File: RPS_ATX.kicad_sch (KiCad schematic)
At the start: 36 parts, among them J1 Fan_in, J13 Fan_out, J2 C1, J3 C2, J4 17.5V, J5 PS_OUT-, J6 PS_OUT+, J7 RPS_OUT+, J9 RPS_OUT-, Q1 AO3400A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

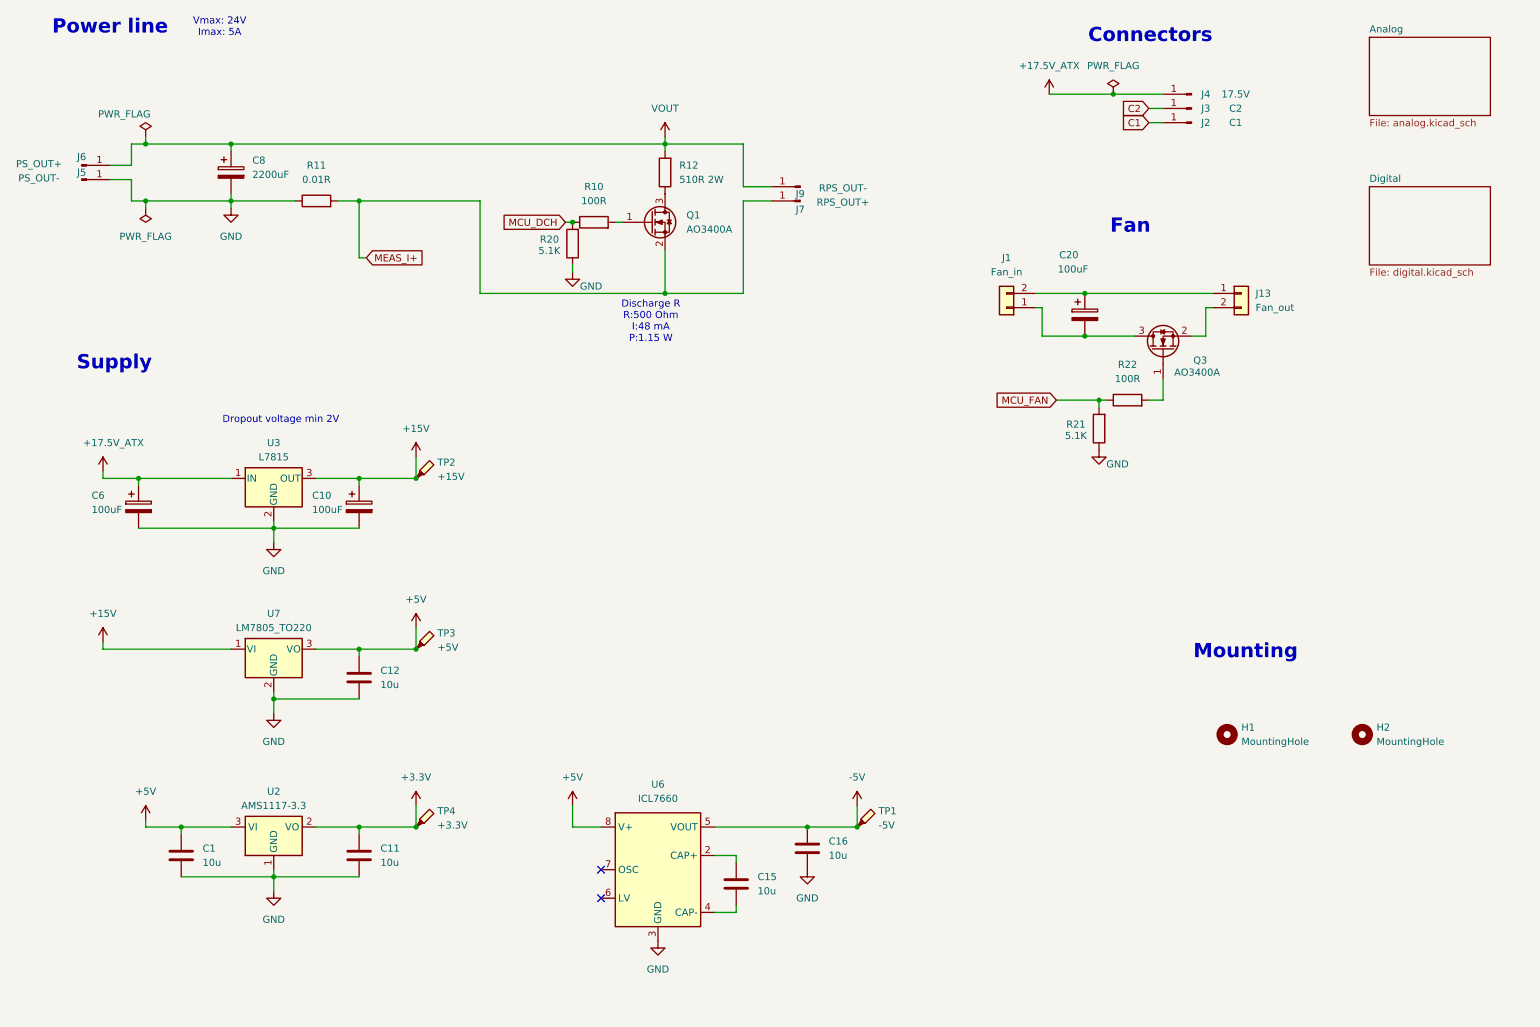
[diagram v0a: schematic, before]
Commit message: fan and temp sensor tracing
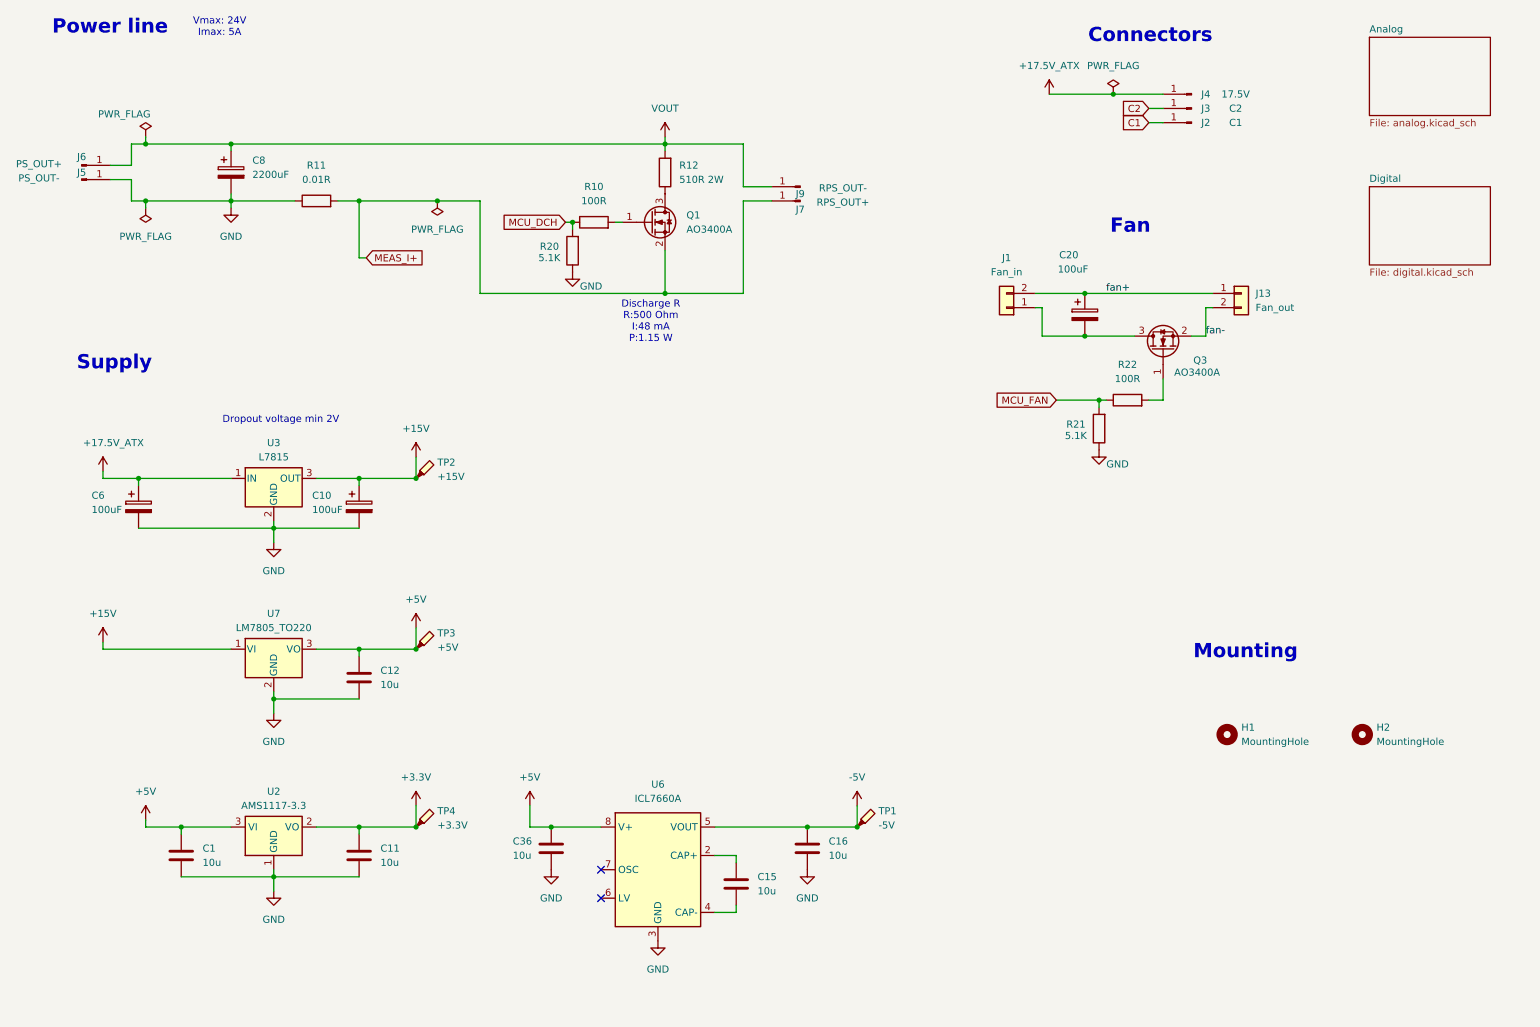
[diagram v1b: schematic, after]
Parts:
- added C36: 10u, Capacitor_SMD:C_1206_3216Metric_Pad1.33x1.80mm_HandSolder, symbol Device:C
- J1, J13: footprint Connector_PinHeader_2.54mm:PinHeader_1x02_P2.54mm_Vertical -> Connector_JST:JST_XH_B2B-XH-A_1x02_P2.50mm_Vertical
- U6: value ICL7660 -> ICL7660A
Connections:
- net +5V: now also C36.1
- net GND: now also C36.2
- net fan+: now reaches C20.1, J1.2 (Pin_2), J13.1 (Pin_1)
- net fan-: now reaches J13.2 (Pin_2), Q3.2 (S)
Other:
- moved on the sheet: R20

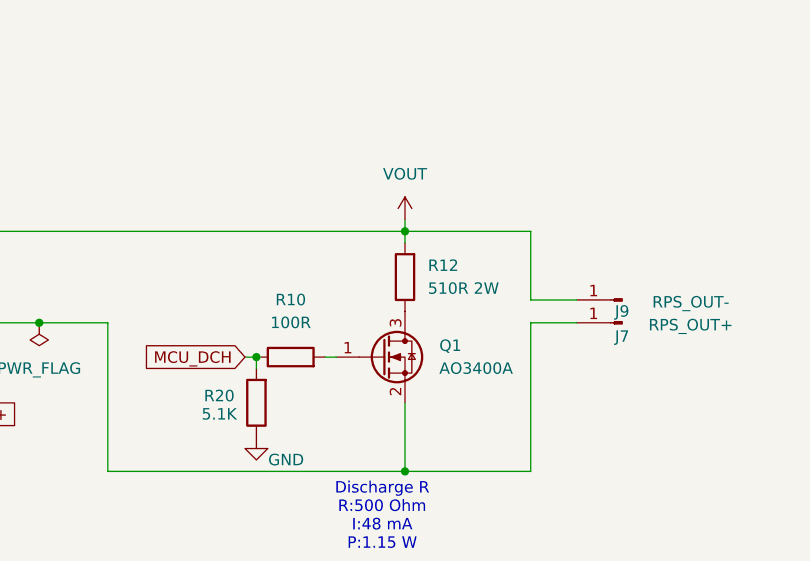
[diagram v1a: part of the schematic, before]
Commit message: minor changes (0805 for 0.1% R, new Y)
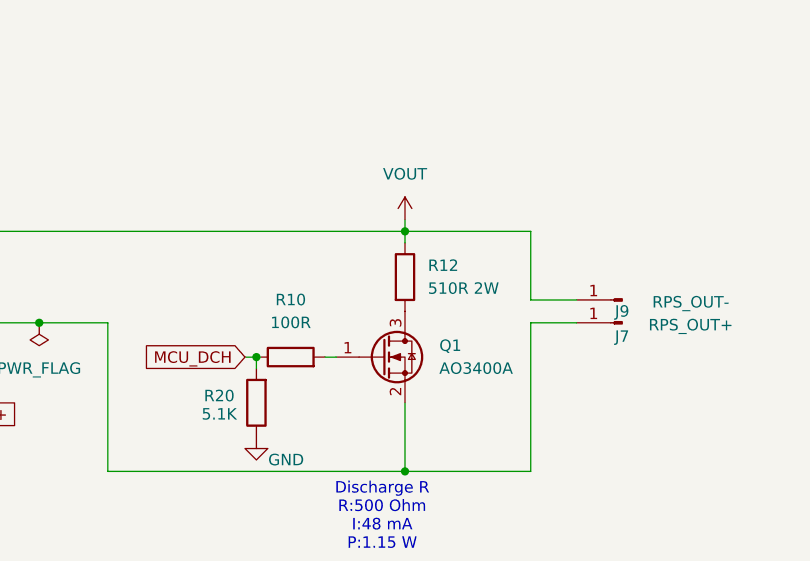
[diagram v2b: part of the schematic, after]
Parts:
- J1, J13: footprint Connector_JST:JST_XH_B2B-XH-A_1x02_P2.50mm_Vertical -> Connector_PinHeader_2.54mm:PinHeader_1x02_P2.54mm_Vertical; now left out of the parts list
- J2, J3, J4, J5, J6, TP1, TP2, TP3, TP4: now left out of the parts list
- J7, J9: footprint Connector_Wire:SolderWire-4sqmm_1x01_D3mm_OD6mm -> Connector_Wire:SolderWire-2sqmm_1x01_D2mm_OD3.9mm; now left out of the parts list
- R12: footprint Resistor_THT:R_Axial_DIN0414_L11.9mm_D4.5mm_P5.08mm_Vertical -> Resistor_THT:R_Axial_Power_L25.0mm_W9.0mm_P7.62mm_Vertical
- R20, R21: footprint Resistor_SMD:R_1206_3216Metric_Pad1.30x1.75mm_HandSolder -> Resistor_SMD:R_0805_2012Metric_Pad1.20x1.40mm_HandSolder
- U3: footprint Package_TO_SOT_SMD:TO-252-3_TabPin2 -> Package_TO_SOT_THT:TO-220-3_Vertical
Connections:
- net VOUT: now also R12.1; no longer R12.2
- net at Q1.3 (D): now also R12.2; no longer R12.1
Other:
- moved on the sheet: R12
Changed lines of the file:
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@@
 		(unit 1)
 		(exclude_from_sim no)
-		(in_bom yes)
+		(in_bom no)
 		(on_board yes)
 		(dnp no)
@@
 			)
 		)
-		(property "Footprint" "Resistor_SMD:R_1206_3216Metric_Pad1.30x1.75mm_HandSolder"
+		(property "Footprint" "Resistor_SMD:R_0805_2012Metric_Pad1.20x1.40mm_HandSolder"
 			(at 207.518 90.17 90)
 			(effects
@@
 		(unit 1)
 		(exclude_from_sim no)
-		(in_bom yes)
+		(in_bom no)
 		(on_board yes)
 		(dnp no)
@@
 		(unit 1)
 		(exclude_from_sim no)
-		(in_bom yes)
+		(in_bom no)
 		(on_board yes)
 		(dnp no)
@@
 			)
 		)
-		(property "Footprint" "Connector_JST:JST_XH_B2B-XH-A_1x02_P2.50mm_Vertical"
+		(property "Footprint" "Connector_PinHeader_2.54mm:PinHeader_1x02_P2.54mm_Vertical"
 			(at 231.14 66.04 0)
 			(effects
@@
 		(unit 1)
 		(exclude_from_sim no)
-		(in_bom yes)
+		(in_bom no)
 		(on_board yes)
 		(dnp no)
@@
 		(unit 1)
 		(exclude_from_sim no)
-		(in_bom yes)
+		(in_bom no)
 		(on_board yes)
 		(dnp no)
@@
 			)
 		)
-		(property "Footprint" "Connector_Wire:SolderWire-4sqmm_1x01_D3mm_OD6mm"
+		(property "Footprint" "Connector_Wire:SolderWire-2sqmm_1x01_D2mm_OD3.9mm"
 			(at 152.4 49.53 0)
 			(effects
@@
 		(unit 1)
 		(exclude_from_sim no)
-		(in_bom yes)
+		(in_bom no)
 		(on_board yes)
 		(dnp no)
@@
 			)
 		)
-		(property "Footprint" "Connector_JST:JST_XH_B2B-XH-A_1x02_P2.50mm_Vertical"
+		(property "Footprint" "Connector_PinHeader_2.54mm:PinHeader_1x02_P2.54mm_Vertical"
 			(at 189.23 68.58 0)
 			(effects
@@
 		(unit 1)
 		(exclude_from_sim no)
-		(in_bom yes)
+		(in_bom no)
 		(on_board yes)
 		(dnp no)
@@
 		(unit 1)
 		(exclude_from_sim no)
-		(in_bom yes)
+		(in_bom no)
 		(on_board yes)
 		(dnp no)
@@
 		(unit 1)
 		(exclude_from_sim no)
-		(in_bom yes)
+		(in_bom no)
 		(on_board yes)
 		(dnp no)
@@
 		(unit 1)
 		(exclude_from_sim no)
-		(in_bom yes)
+		(in_bom no)
 		(on_board yes)
 		(dnp no)
@@
 		(unit 1)
 		(exclude_from_sim no)
-		(in_bom yes)
+		(in_bom no)
 		(on_board yes)
 		(dnp no)
@@
 			)
 		)
-		(property "Footprint" "Connector_Wire:SolderWire-4sqmm_1x01_D3mm_OD6mm"
+		(property "Footprint" "Connector_Wire:SolderWire-2sqmm_1x01_D2mm_OD3.9mm"
 			(at 152.4 46.99 0)
 			(effects
@@
 	(symbol
 		(lib_id "Device:R")
-		(at 128.27 44.45 180)
+		(at 128.27 44.45 0)
 		(unit 1)
 		(exclude_from_sim no)
@@
 					(size 1.27 1.27)
 				)
-				(justify right)
+				(justify left)
 			)
 		)
@@
 					(size 1.27 1.27)
 				)
-				(justify right)
+				(justify left)
 			)
 		)
-		(property "Footprint" "Resistor_THT:R_Axial_DIN0414_L11.9mm_D4.5mm_P5.08mm_Vertical"
-			(at 130.048 44.45 90)
+		(property "Footprint" "Resistor_THT:R_Axial_Power_L25.0mm_W9.0mm_P7.62mm_Vertical"
+			(at 126.492 44.45 90)
 			(effects
 				(font
@@
 			)
 		)
-		(property "Footprint" "Resistor_SMD:R_1206_3216Metric_Pad1.30x1.75mm_HandSolder"
+		(property "Footprint" "Resistor_SMD:R_0805_2012Metric_Pad1.20x1.40mm_HandSolder"
 			(at 113.538 58.42 90)
 			(effects
@@
 			)
 		)
-		(property "Footprint" "Package_TO_SOT_SMD:TO-252-3_TabPin2"
+		(property "Footprint" "Package_TO_SOT_THT:TO-220-3_Vertical"
 			(at 59.055 102.87 0)
 			(effects
@@
 		(unit 1)
 		(exclude_from_sim no)
-		(in_bom yes)
+		(in_bom no)
 		(on_board yes)
 		(dnp no)
@@
 		(unit 1)
 		(exclude_from_sim no)
-		(in_bom yes)
+		(in_bom no)
 		(on_board yes)
 		(dnp no)

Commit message: changing concept
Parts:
- removed C1, C11, C15, C16, C36: 10u, Capacitor_SMD:C_1206_3216Metric_Pad1.33x1.80mm_HandSolder, symbol Device:C
- removed Q1: AO3400A, Package_TO_SOT_SMD:SOT-23, symbol Transistor_FET:AO3400A
- removed R10: 100R, Resistor_SMD:R_1206_3216Metric_Pad1.30x1.75mm_HandSolder, symbol Device:R
- removed R20: 5.1K, Resistor_SMD:R_0805_2012Metric_Pad1.20x1.40mm_HandSolder, symbol Device:R
- removed TP1: -5V, TestPoint:TestPoint_Pad_D2.0mm, symbol Connector:TestPoint_Probe
- removed TP4: +3.3V, TestPoint:TestPoint_Pad_D2.0mm, symbol Connector:TestPoint_Probe
- removed U2: AMS1117-3.3, Package_TO_SOT_SMD:SOT-223-3_TabPin2, symbol Regulator_Linear:AMS1117-3.3
- removed U6: ICL7660A, Package_DIP:DIP-8_W7.62mm, symbol Regulator_SwitchedCapacitor:ICL7660
- added R2: 0.005R, my lib:Resistor_Shunt_L10_D3.7, symbol Device:R
- added U2: Mini360, symbol mini360:Mini360
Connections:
- net +15V: now also U2.2 (IN+); no longer U7.1 (VI)
- net GND: now also U2.1 (IN-), U2.3 (OUT-)
- net MEAS_I+: now also R12.2, R2.1; no longer J7.1 (Pin_1)
- new net: J7.1 (Pin_1), R2.2
- new net +8V: U2.4 (OUT+), U7.1 (VI)
- no-connect marks 2 -> 0
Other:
- removed sheet Digital
- note added: "Vmax: 25V Imax: 5A"
- note removed: "Discharge R R:500 Ohm I:48 mA P:1.15 W"
- note removed: "Vmax: 24V Imax: 5A"
- moved on the sheet: C12, R12, TP3, U7

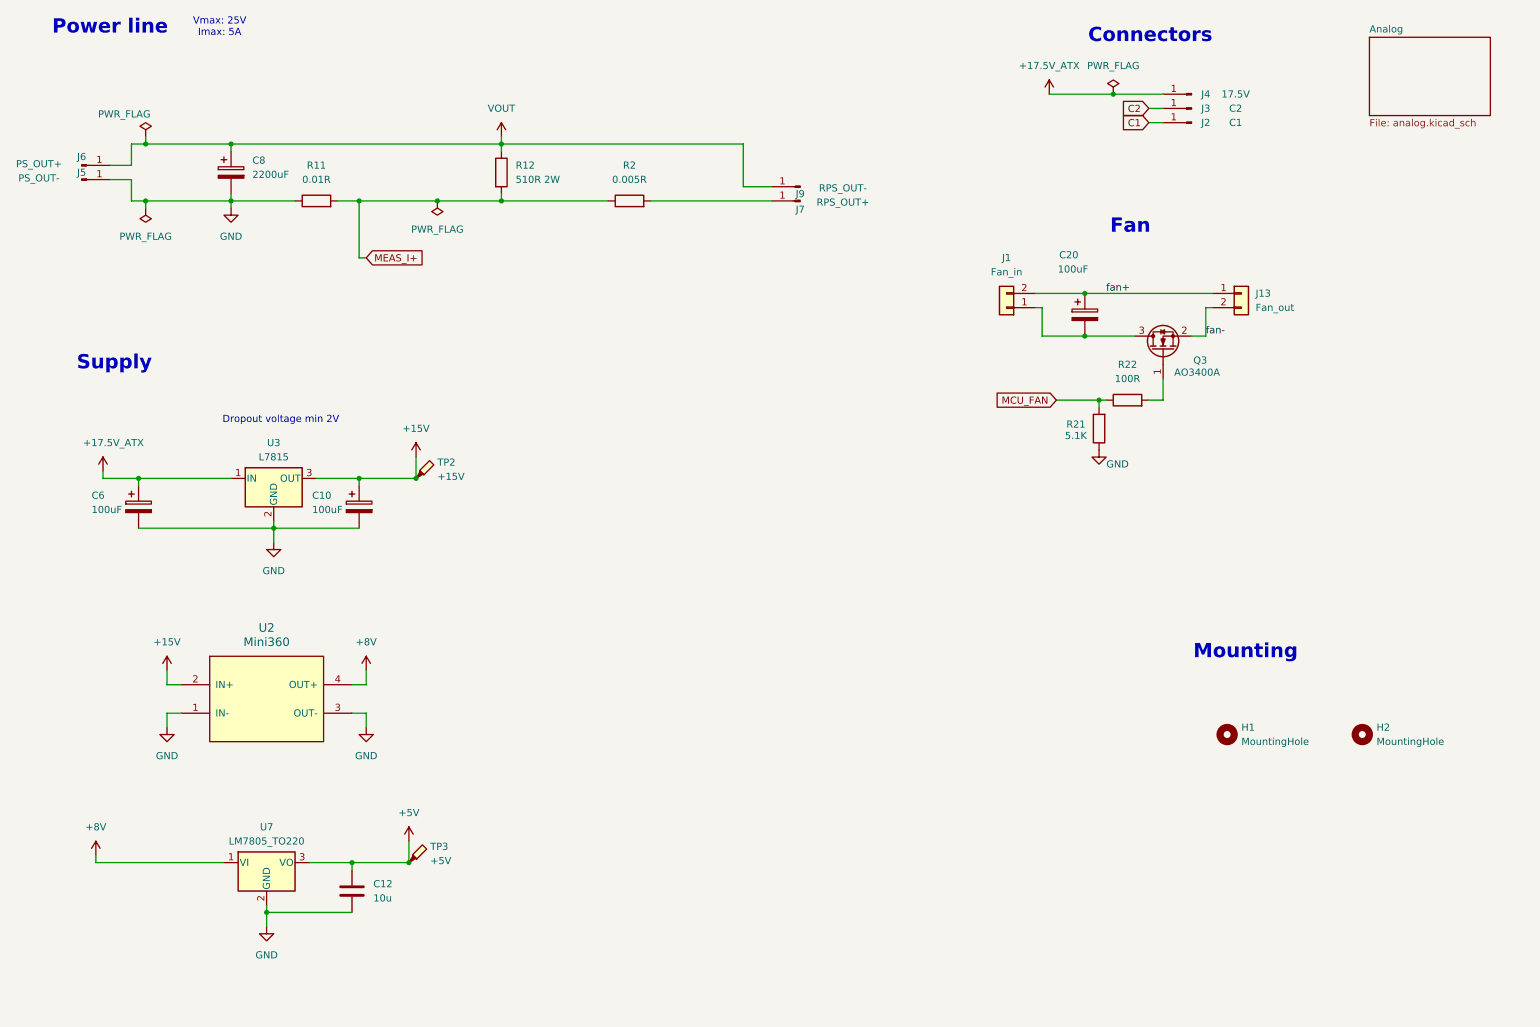
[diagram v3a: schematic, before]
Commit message: excluding STM32G431
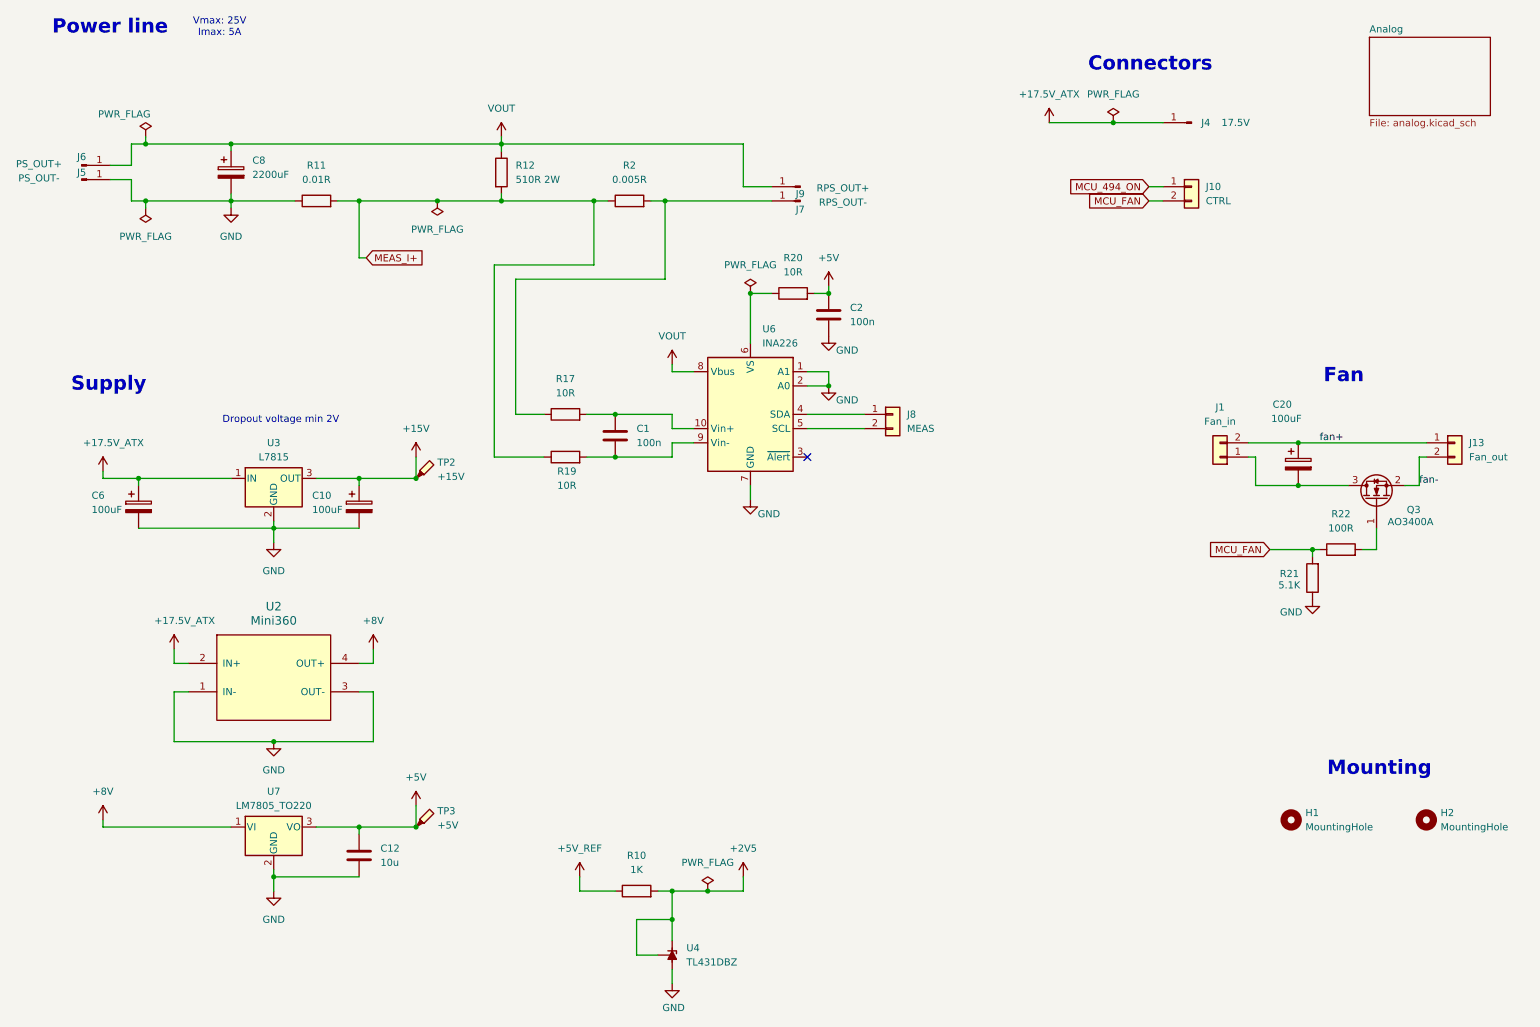
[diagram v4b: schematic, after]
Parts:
- removed J2: C1, Connector_PinHeader_2.54mm:PinHeader_1x01_P2.54mm_Vertical, symbol Connector:Conn_01x01_Pin
- removed J3: C2, Connector_PinHeader_2.54mm:PinHeader_1x01_P2.54mm_Vertical, symbol Connector:Conn_01x01_Pin
- added C1, C2: 100n, Capacitor_SMD:C_0805_2012Metric_Pad1.18x1.45mm_HandSolder, symbol Device:C
- added J10: CTRL, Connector_PinHeader_2.54mm:PinHeader_1x02_P2.54mm_Vertical, symbol Connector_Generic:Conn_01x02
- added J8: MEAS, Connector_PinHeader_2.54mm:PinHeader_1x02_P2.54mm_Vertical, symbol Connector_Generic:Conn_01x02
- added R10: 1K, Resistor_SMD:R_1206_3216Metric_Pad1.30x1.75mm_HandSolder, symbol Device:R
- added R17, R19, R20: 10R, Resistor_SMD:R_1206_3216Metric_Pad1.30x1.75mm_HandSolder, symbol Device:R
- added U4: TL431DBZ, Package_TO_SOT_SMD:SOT-23, symbol Reference_Voltage:TL431DBZ
- added U6: INA226, Package_SO:VSSOP-10_3x3mm_P0.5mm, symbol Sensor_Energy:INA226
- J7: value RPS_OUT+ -> RPS_OUT-
- J9: value RPS_OUT- -> RPS_OUT+
- R2: footprint my lib:Resistor_Shunt_L10_D3.7 -> MyLibrary:Shunt 0.005R
- U2: footprint (none) -> Mini360_step-down:Mini360_step-down
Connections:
- net +15V: no longer U2.2 (IN+)
- net +17.5V_ATX: now also U2.2 (IN+)
- net +5V: now also C2.1, R20.2
- net GND: now also C2.2, U4.3 (A), U6.1 (A1), U6.2 (A0), U6.7 (GND)
- net MCU_FAN: now also J10.2 (Pin_2)
- net MEAS_I+: now also R19.1
- net VOUT: now also U6.8 (Vbus)
- net at J7.1 (Pin_1), R2.2: now also R17.1
- new net: C1.1, R17.2, U6.10 (Vin+)
- new net: J8.1 (Pin_1), U6.4 (SDA)
- new net: J8.2 (Pin_2), U6.5 (SCL)
- new net: R20.1, U6.6 (VS)
- new net: C1.2, R19.2, U6.9 (Vin-)
- new net +2V5: R10.2, U4.1 (K), U4.2 (REF)
- new net +5V_REF: R10.1
- new net MCU_494_ON: J10.1 (Pin_1)
- no-connect marks 0 -> 1
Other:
- moved on the sheet: C12, C20, H1, H2, J1, J13, J4, Q3, R21, R22, TP3, U2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
